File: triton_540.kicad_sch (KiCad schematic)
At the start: 46 parts, among them J1 REC ANT, J3 Conn_01x04, J4 AUX 12V, J5 KEY, J6 PTT, Q2 MPS6514, Y1 13.99MHz, Y2 14.49MHz, Y3 14.99MHz, Y4 15.49MHz

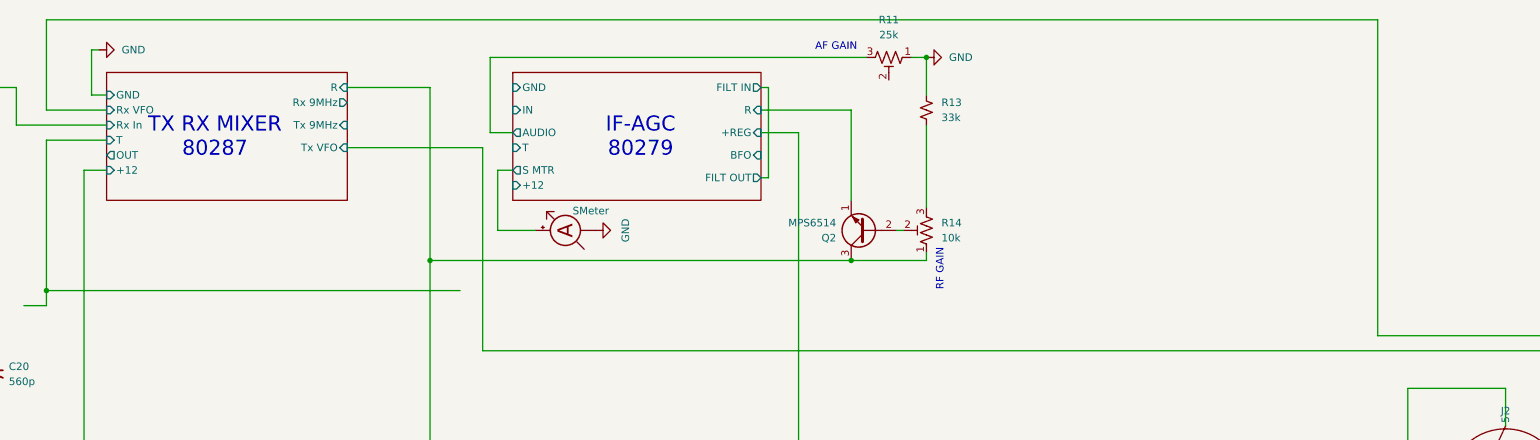
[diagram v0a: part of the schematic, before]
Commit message: add 80274 audio power amplifier
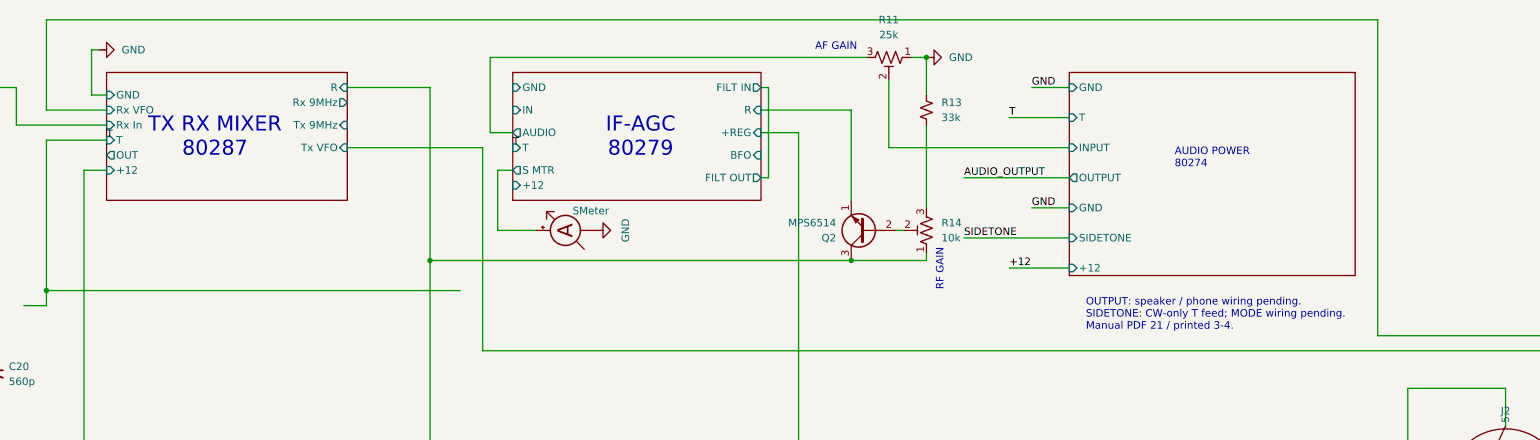
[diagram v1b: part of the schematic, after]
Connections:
- net Audio_Power_80274/INPUT: now reaches R11.2
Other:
- added sheet Audio_Power_80274 (80274_audio_power_amp.kicad_sch)
- note added: "AUDIO POWER 80274"
- note added: "OUTPUT: speaker / phone wiring pending. SIDETONE: CW-only T feed; MODE wiring pending. Manual PDF 21 / printed 3-4."
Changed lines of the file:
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@@
 		)
 	)
+(sheet (at 330.2 25.4) (size 48.26 34.29) (exclude_from_sim yes) (in_bom yes) (on_board yes) (dnp no) (stroke (width 0.1524) (type solid)) (fill (color 0 0 0 0)) (property "Sheetname" "Audio_Power_80274" (at 330.2 24.6884 0) (hide yes) (effects (font (size 1.27 1.27)) (justify left bottom))) (property "Sheetfile" "80274_audio_power_amp.kicad_sch" (at 330.2 60.4 0) (hide yes) (effects (font (size 1.27 1.27)) (justify left top)))(pin "GND" input (at 330.2 27.94 180) (effects (font (size 1.27 1.27)) (justify left)))(pin "T" input (at 330.2 33.02 180) (effects (font (size 1.27 1.27)) (justify left)))(pin "INPUT" input (at 330.2 38.1 180) (effects (font (size 1.27 1.27)) (justify left)))(pin "OUTPUT" output (at 330.2 43.18 180) (effects (font (size 1.27 1.27)) (justify left)))(pin "GND" input (at 330.2 48.26 180) (effects (font (size 1.27 1.27)) (justify left)))(pin "SIDETONE" input (at 330.2 53.34 180) (effects (font (size 1.27 1.27)) (justify left)))(pin "+12" input (at 330.2 58.42 180) (effects (font (size 1.27 1.27)) (justify left)))(instances (project "triton_540" (path "/2d45daab-5f60-4e97-8c02-32b0054eab28" (page "6")))))
+(text "AUDIO POWER\n80274" (at 347.98 38.1 0) (effects (font (size 1.27 1.27)) (justify left top)))
+(wire (pts (xy 299.72 26.67) (xy 299.72 38.1)) (stroke (width 0) (type default)))
+(wire (pts (xy 299.72 38.1) (xy 330.2 38.1)) (stroke (width 0) (type default)))
+(wire (pts (xy 330.2 58.42) (xy 320.04 58.42)) (stroke (width 0) (type default)))
+(label "+12" (at 320.04 58.42 0) (effects (font (size 1.27 1.27)) (justify left bottom)))
+(wire (pts (xy 330.2 33.02) (xy 320.04 33.02)) (stroke (width 0) (type default)))
+(label "T" (at 320.04 33.02 0) (effects (font (size 1.27 1.27)) (justify left bottom)))
+(label "T" (at 236.22 38.1 0) (effects (font (size 1.27 1.27)) (justify left bottom)))
+(label "T" (at 167.64 36.83 0) (effects (font (size 1.27 1.27)) (justify left bottom)))
+(wire (pts (xy 330.2 27.94) (xy 323.85 27.94)) (stroke (width 0) (type default)))
+(label "GND" (at 323.85 27.94 0) (effects (font (size 1.27 1.27)) (justify left bottom)))
+(wire (pts (xy 330.2 48.26) (xy 323.85 48.26)) (stroke (width 0) (type default)))
+(label "GND" (at 323.85 48.26 0) (effects (font (size 1.27 1.27)) (justify left bottom)))
+(wire (pts (xy 330.2 43.18) (xy 312.42 43.18)) (stroke (width 0) (type default)))
+(label "AUDIO_OUTPUT" (at 312.42 43.18 0) (effects (font (size 1.27 1.27)) (justify left bottom)))
+(wire (pts (xy 330.2 53.34) (xy 312.42 53.34)) (stroke (width 0) (type default)))
+(label "SIDETONE" (at 312.42 53.34 0) (effects (font (size 1.27 1.27)) (justify left bottom)))
+(text "OUTPUT: speaker / phone wiring pending.\nSIDETONE: CW-only T feed; MODE wiring pending.\nManual PDF 21 / printed 3-4." (at 333 63.5 0) (effects (font (size 1.27 1.27)) (justify left top)))
 	(sheet_instances
 		(path "/"
